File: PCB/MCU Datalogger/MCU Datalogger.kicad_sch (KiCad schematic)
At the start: 25 parts, among them U1 24LC1025, U2 24LC1025, U3 DS1337S+, U4 ATMEGA328P-AU, Y1 Crystal, Y2 Crystal

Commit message: edit component values
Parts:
- C1, C4: value C -> 0.1uF
- C2, C3: value C -> 22pF
- C5: value C_Polarized -> 100nF
- R1, R2: value R -> 330
- R3, R4, R7: value R -> 10K
- R5, R6: value R -> 4.7K
- Y1: value Crystal -> 16 MHz
- Y2: value Crystal -> 32.768 Khz
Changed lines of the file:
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@@
       (effects (font (size 1.27 1.27)) (justify left))
     )
-    (property "Value" "C" (at 163.83 81.28 0)
+    (property "Value" "22pF" (at 163.83 81.28 0)
       (effects (font (size 1.27 1.27)) (justify left))
     )
@@
       (effects (font (size 1.27 1.27)) (justify left))
     )
-    (property "Value" "R" (at 102.87 54.61 0)
+    (property "Value" "10K" (at 102.87 54.61 0)
       (effects (font (size 1.27 1.27)) (justify left))
     )
@@
       (effects (font (size 1.27 1.27)) (justify left))
     )
-    (property "Value" "R" (at 130.81 184.15 0)
+    (property "Value" "4.7K" (at 130.81 184.15 0)
       (effects (font (size 1.27 1.27)) (justify left))
     )
@@
       (effects (font (size 1.27 1.27)) (justify right))
     )
-    (property "Value" "Crystal" (at 181.61 68.58 90)
+    (property "Value" "16 MHz" (at 181.61 68.58 90)
       (effects (font (size 1.27 1.27)) (justify right))
     )
@@
       (effects (font (size 1.27 1.27)) (justify left))
     )
-    (property "Value" "R" (at 90.17 54.61 0)
+    (property "Value" "10K" (at 90.17 54.61 0)
       (effects (font (size 1.27 1.27)) (justify left))
     )
@@
       (effects (font (size 1.27 1.27)) (justify left))
     )
-    (property "Value" "C" (at 116.84 54.61 0)
+    (property "Value" "0.1uF" (at 116.84 54.61 0)
       (effects (font (size 1.27 1.27)) (justify left))
     )
@@
       (effects (font (size 1.27 1.27)) (justify left))
     )
-    (property "Value" "C_Polarized" (at 252.73 43.561 0)
+    (property "Value" "100nF" (at 252.73 43.561 0)
       (effects (font (size 1.27 1.27)) (justify left))
     )
@@
       (effects (font (size 1.27 1.27)) (justify left))
     )
-    (property "Value" "C" (at 168.91 30.48 0)
+    (property "Value" "0.1uF" (at 168.91 30.48 0)
       (effects (font (size 1.27 1.27)) (justify left))
     )
@@
       (effects (font (size 1.27 1.27)) (justify left))
     )
-    (property "Value" "R" (at 120.65 184.15 0)
+    (property "Value" "4.7K" (at 120.65 184.15 0)
       (effects (font (size 1.27 1.27)) (justify left))
     )
@@
       (effects (font (size 1.27 1.27)) (justify left))
     )
-    (property "Value" "R" (at 240.03 71.12 0)
+    (property "Value" "330" (at 240.03 71.12 0)
       (effects (font (size 1.27 1.27)) (justify left))
     )
@@
       (effects (font (size 1.27 1.27)))
     )
-    (property "Value" "R" (at 158.75 40.64 90)
+    (property "Value" "330" (at 158.75 40.64 90)
       (effects (font (size 1.27 1.27)))
     )
@@
       (effects (font (size 1.27 1.27)) (justify right))
     )
-    (property "Value" "Crystal" (at 25.4 63.5 90)
+    (property "Value" "32.768 Khz" (at 25.4 63.5 90)
       (effects (font (size 1.27 1.27)) (justify right))
     )
@@
       (effects (font (size 1.27 1.27)))
     )
-    (property "Value" "R" (at 177.8 80.01 90)
+    (property "Value" "10K" (at 177.8 80.01 90)
       (effects (font (size 1.27 1.27)))
     )
@@
       (effects (font (size 1.27 1.27)) (justify left))
     )
-    (property "Value" "C" (at 163.83 60.96 0)
-      (effects (font (size 1.27 1.27)) (justify left))
-    )
+    (property "Value" "22pF" (at 163.83 60.96 0)
+      (effects (font (size 1.27 1.27)) (justify left))
+    )

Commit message: Associate
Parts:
- BT1: footprint (none) -> Connector_PinHeader_2.54mm:PinHeader_1x02_P2.54mm_Vertical
- C1, C2, C3, C4, C5: footprint (none) -> Capacitor_SMD:C_0805_2012Metric
- D1, D2: footprint (none) -> LED_SMD:LED_0805_2012Metric
- H1, H2, H3, H4: footprint (none) -> MountingHole:MountingHole_2.1mm
- R1, R2, R3, R4, R5, R6, R7: footprint (none) -> Resistor_SMD:R_0815_2038Metric
- U1, U2: footprint (none) -> Package_SO:SOIC-8_5.23x5.23mm_P1.27mm
- U3: footprint SOIC127P600X175-8N -> DS1337S_:SOIC127P600X175-8N
- U4: footprint QFP80P900X900X120-32N -> ATMEGA328P-AU:QFP80P900X900X120-32N
- Y1, Y2: footprint (none) -> Crystal:Crystal_SMD_5032-2Pin_5.0x3.2mm_HandSoldering
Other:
- moved on the sheet: BT1, C1, C2, C3, C5, D1, D2, R1, R2, R5, R6, R7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

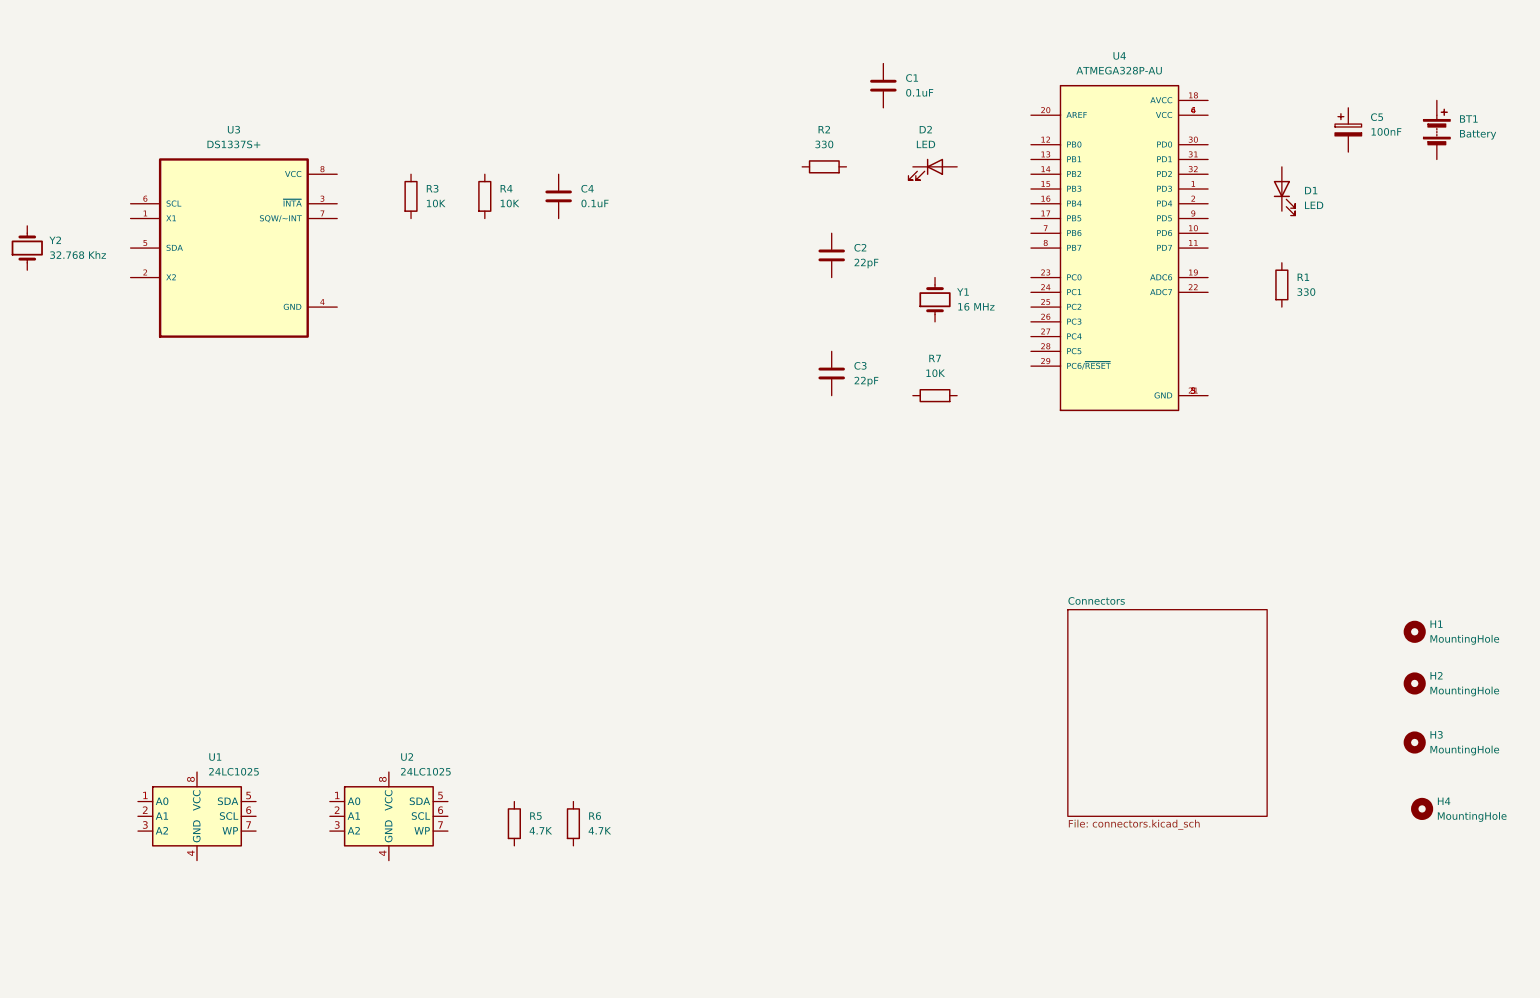
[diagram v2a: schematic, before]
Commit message: wiring of sheet 1
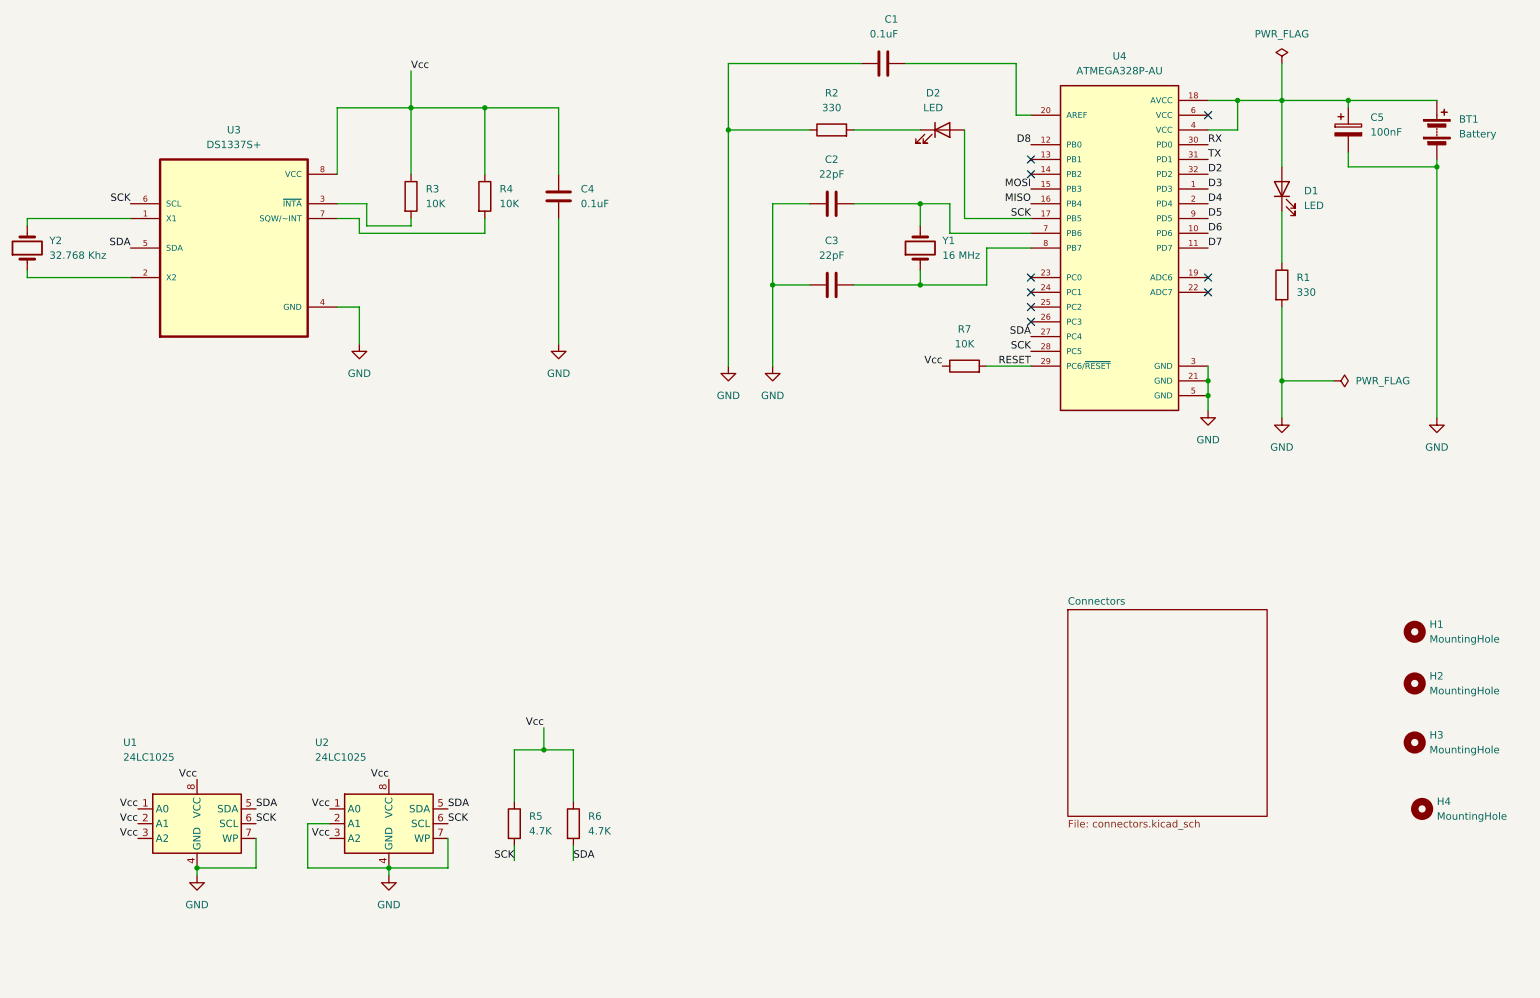
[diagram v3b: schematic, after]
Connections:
- net GND: now reaches C3.1
- net GND: now also BT1.2 (-), C1.1, C2.1, C4.2, C5.2, R1.2, R2.1, U1.4 (GND), U1.7 (WP), U2.2 (A1), U2.4 (GND), U2.7 (WP), U3.4 (GND), U4.21 (GND), U4.3 (GND), U4.5 (GND)
- net at C3.2: now also U4.8 (PB7), Y1.1
- net Vcc: now reaches R4.1
- net Vcc: now also C4.1, R3.1, R5.1, R6.1, R7.1, U1.1 (A0), U1.2 (A1), U1.3 (A2), U1.8 (VCC), U2.1 (A0), U2.3 (A2), U2.8 (VCC), U3.8 (VCC)
- net at R4.2: now also U3.7 (SQW/~INT)
- net SDA: now reaches U1.5 (SDA)
- net SDA: now also R6.2, U2.5 (SDA), U3.5 (SDA), U4.27 (PC4)
- net SCK: now reaches U1.6 (SCL)
- net SCK: now also D2.2 (A), R5.2, U2.6 (SCL), U3.6 (SCL), U4.17 (PB5), U4.28 (PC5)
- net at Y1.2: now also C2.2, U4.7 (PB6)
- net at R3.2: now also U3.3 (~{INTA})
- net at C5.1: now also BT1.1 (+), D1.2 (A), U4.18 (AVCC), U4.4 (VCC)
- net at C1.2: now also U4.20 (AREF)
- net at D2.1 (K): now also R2.2
- net at R1.1: now also D1.1 (K)
- net at Y2.1: now also U3.2 (X2)
- net at Y2.2: now also U3.1 (X1)
- net RESET: now reaches R7.2
- net RESET: now also U4.29 (PC6/~{RESET})
- net D3: now reaches U4.1 (PD3)
- net D6: now reaches U4.10 (PD6)
- net D7: now reaches U4.11 (PD7)
- net D8: now reaches U4.12 (PB0)
- net MOSI: now reaches U4.15 (PB3)
- net MISO: now reaches U4.16 (PB4)
- net D4: now reaches U4.2 (PD4)
- net RX: now reaches U4.30 (PD0)
- net TX: now reaches U4.31 (PD1)
- net D2: now reaches U4.32 (PD2)
- net at U4.6 (VCC): no longer U4.4 (VCC)
- net D5: now reaches U4.9 (PD5)
- no-connect marks 0 -> 9
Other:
- moved on the sheet: C1, C2, C3, D2, R2, R7, U1, U2, Y1

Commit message: Wiring of sheet 2
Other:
- sheet Connectors ports: added D2, D3, D4, D5, D6, D7, D8, GND, MISO, MOSI, RESET, RX, SCK, SDA, TX, Vcc; removed none
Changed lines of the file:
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@@
   (junction (at 149.86 68.58) (diameter 0) (color 0 0 0 0)
+  )
+  (junction (at 105.41 38.1) (diameter 0) (color 0 0 0 0)
   )
   (junction (at 50.8 168.91) (diameter 0) (color 0 0 0 0)
@@
     (stroke (width 0) (type default))
   )
+  (wire (pts (xy 105.41 38.1) (xy 113.03 38.1))
+    (stroke (width 0) (type default))
+  )
   (wire (pts (xy 105.41 157.48) (xy 105.41 148.59))
     (stroke (width 0) (type default))
@@
     (stroke (width 0) (type default))
   )
-  (wire (pts (xy 100.33 38.1) (xy 113.03 38.1))
+  (wire (pts (xy 100.33 38.1) (xy 105.41 38.1))
     (stroke (width 0) (type default))
   )
@@
     (stroke (width 0) (type default))
   )
+  (wire (pts (xy 105.41 33.02) (xy 105.41 38.1))
+    (stroke (width 0) (type default))
+  )
   (wire (pts (xy 156.21 54.61) (xy 149.86 54.61))
     (stroke (width 0) (type default))
@@
     (effects (font (size 1.27 1.27)) (justify left bottom))
   )
+  (label "D3" (at 213.36 124.46 0) (fields_autoplaced)
+    (effects (font (size 1.27 1.27)) (justify left bottom))
+  )
   (label "MOSI" (at 194.31 52.07 180) (fields_autoplaced)
     (effects (font (size 1.27 1.27)) (justify right bottom))
   )
+  (label "D6" (at 213.36 135.89 0) (fields_autoplaced)
+    (effects (font (size 1.27 1.27)) (justify left bottom))
+  )
   (label "Vcc" (at 179.07 82.55 180) (fields_autoplaced)
     (effects (font (size 1.27 1.27)) (justify right bottom))
@@
     (effects (font (size 1.27 1.27)) (justify right bottom))
   )
+  (label "SCK" (at 182.88 121.92 180) (fields_autoplaced)
+    (effects (font (size 1.27 1.27)) (justify right bottom))
+  )
   (label "SCK" (at 105.41 167.64 180) (fields_autoplaced)
     (effects (font (size 1.27 1.27)) (justify right bottom))
   )
+  (label "MOSI" (at 182.88 146.05 180) (fields_autoplaced)
+    (effects (font (size 1.27 1.27)) (justify right bottom))
+  )
+  (label "D2" (at 213.36 120.65 0) (fields_autoplaced)
+    (effects (font (size 1.27 1.27)) (justify left bottom))
+  )
+  (label "D8" (at 213.36 143.51 0) (fields_autoplaced)
+    (effects (font (size 1.27 1.27)) (justify left bottom))
+  )
+  (label "D7" (at 213.36 139.7 0) (fields_autoplaced)
+    (effects (font (size 1.27 1.27)) (justify left bottom))
+  )
   (label "SDA" (at 115.57 167.64 0) (fields_autoplaced)
     (effects (font (size 1.27 1.27)) (justify left bottom))
   )
+  (label "D5" (at 213.36 132.08 0) (fields_autoplaced)
+    (effects (font (size 1.27 1.27)) (justify left bottom))
+  )
   (label "SCK" (at 60.96 161.29 0) (fields_autoplaced)
     (effects (font (size 1.27 1.27)) (justify left bottom))
@@
     (effects (font (size 1.27 1.27)) (justify right bottom))
   )
+  (label "RESET" (at 182.88 153.67 180) (fields_autoplaced)
+    (effects (font (size 1.27 1.27)) (justify right bottom))
+  )
   (label "D6" (at 224.79 59.69 0) (fields_autoplaced)
     (effects (font (size 1.27 1.27)) (justify left bottom))
@@
     (effects (font (size 1.27 1.27)) (justify right bottom))
   )
+  (label "Vcc" (at 182.88 111.76 180) (fields_autoplaced)
+    (effects (font (size 1.27 1.27)) (justify right bottom))
+  )
   (label "Vcc" (at 73.66 158.75 180) (fields_autoplaced)
     (effects (font (size 1.27 1.27)) (justify right bottom))
@@
     (effects (font (size 1.27 1.27)) (justify right bottom))
   )
+  (label "D4" (at 213.36 128.27 0) (fields_autoplaced)
+    (effects (font (size 1.27 1.27)) (justify left bottom))
+  )
   (label "SDA" (at 93.98 158.75 0) (fields_autoplaced)
     (effects (font (size 1.27 1.27)) (justify left bottom))
@@
     (effects (font (size 1.27 1.27)) (justify right bottom))
   )
+  (label "SDA" (at 182.88 125.73 180) (fields_autoplaced)
+    (effects (font (size 1.27 1.27)) (justify right bottom))
+  )
+  (label "RX" (at 182.88 134.62 180) (fields_autoplaced)
+    (effects (font (size 1.27 1.27)) (justify right bottom))
+  )
+  (label "MISO" (at 182.88 149.86 180) (fields_autoplaced)
+    (effects (font (size 1.27 1.27)) (justify right bottom))
+  )
   (label "D4" (at 224.79 54.61 0) (fields_autoplaced)
     (effects (font (size 1.27 1.27)) (justify left bottom))
@@
     (effects (font (size 1.27 1.27)) (justify left bottom))
   )
+  (label "TX" (at 182.88 138.43 180) (fields_autoplaced)
+    (effects (font (size 1.27 1.27)) (justify right bottom))
+  )
   (label "MISO" (at 194.31 54.61 180) (fields_autoplaced)
     (effects (font (size 1.27 1.27)) (justify right bottom))
@@
         (path "/551e4e84-b335-467b-846f-a0d4917bd2bc"
           (reference "#PWR09") (unit 1)
+        )
+      )
+    )
+  )
+  (symbol (lib_id "power:PWR_FLAG") (at 105.41 33.02 0) (unit 1)
+    (in_bom yes) (on_board yes) (dnp no) (fields_autoplaced)
+    (property "Reference" "#FLG03" (at 105.41 31.115 0)
+      (effects (font (size 1.27 1.27)) hide)
+    )
+    (property "Value" "PWR_FLAG" (at 105.41 27.94 0)
+      (effects (font (size 1.27 1.27)))
+    )
+    (property "Footprint" "" (at 105.41 33.02 0)
+      (effects (font (size 1.27 1.27)) hide)
+    )
+    (property "Datasheet" "~" (at 105.41 33.02 0)
+      (effects (font (size 1.27 1.27)) hide)
+    )
+    (pin "1")
+    (instances
+      (project "MCU Datalogger"
+        (path "/551e4e84-b335-467b-846f-a0d4917bd2bc"
+          (reference "#FLG03") (unit 1)
         )
       )
@@
         (path "/551e4e84-b335-467b-846f-a0d4917bd2bc"
           (reference "R2") (unit 1)
+        )
+      )
+    )
+  )
+  (symbol (lib_id "power:GND") (at 182.88 114.3 270) (unit 1)
+    (in_bom yes) (on_board yes) (dnp no) (fields_autoplaced)
+    (property "Reference" "#PWR010" (at 176.53 114.3 0)
+      (effects (font (size 1.27 1.27)) hide)
+    )
+    (property "Value" "GND" (at 179.07 114.3 90)
+      (effects (font (size 1.27 1.27)) (justify right))
+    )
+    (property "Footprint" "" (at 182.88 114.3 0)
+      (effects (font (size 1.27 1.27)) hide)
+    )
+    (property "Datasheet" "" (at 182.88 114.3 0)
+      (effects (font (size 1.27 1.27)) hide)
+    )
+    (pin "1")
+    (instances
+      (project "MCU Datalogger"
+        (path "/551e4e84-b335-467b-846f-a0d4917bd2bc"
+          (reference "#PWR010") (unit 1)
         )
       )
@@
     )
   )
-  (sheet (at 200.66 124.46) (size 34.29 35.56) (fields_autoplaced)
+  (sheet (at 182.88 107.95) (size 30.48 49.53) (fields_autoplaced)
     (stroke (width 0.1524) (type solid))
     (fill (color 0 0 0 0.0000))
-    (property "Sheetname" "Connectors" (at 200.66 123.7484 0)
+    (property "Sheetname" "Connectors" (at 182.88 107.2384 0)
       (effects (font (size 1.27 1.27)) (justify left bottom))
     )
-    (property "Sheetfile" "connectors.kicad_sch" (at 200.66 160.6046 0)
+    (property "Sheetfile" "connectors.kicad_sch" (at 182.88 158.0646 0)
       (effects (font (size 1.27 1.27)) (justify left top))
     )
-    (instances
+    (pin "RX" input (at 182.88 134.62 180)
+      (effects (font (size 1.27 1.27)) (justify left))
+    )
+    (pin "Vcc" passive (at 182.88 111.76 180)
+      (effects (font (size 1.27 1.27)) (justify left))
+    )
+    (pin "TX" output (at 182.88 138.43 180)
+      (effects (font (size 1.27 1.27)) (justify left))
+    )
+    (pin "GND" passive (at 182.88 114.3 180)
+      (effects (font (size 1.27 1.27)) (justify left))
+    )
+    (pin "D4" bidirectional (at 213.36 128.27 0)
+      (effects (font (size 1.27 1.27)) (justify right))
+    )
+    (pin "D2" bidirectional (at 213.36 120.65 0)
+      (effects (font (size 1.27 1.27)) (justify right))
+    )
+    (pin "D8" bidirectional (at 213.36 143.51 0)
+      (effects (font (size 1.27 1.27)) (justify right))
+    )
+    (pin "SCK" passive (at 182.88 121.92 180)
+      (effects (font (size 1.27 1.27)) (justify left))
+    )
+    (pin "SDA" bidirectional (at 182.88 125.73 180)
+      (effects (font (size 1.27 1.27)) (justify left))
+    )
+    (pin "D3" bidirectional (at 213.36 124.46 0)
+      (effects (font (size 1.27 1.27)) (justify right))
+    )
+    (pin "D5" bidirectional (at 213.36 132.08 0)
+      (effects (font (size 1.27 1.27)) (justify right))
+    )
+    (pin "D6" bidirectional (at 213.36 135.89 0)
+      (effects (font (size 1.27 1.27)) (justify right))
+    )
+    (pin "D7" bidirectional (at 213.36 139.7 0)
+      (effects (font (size 1.27 1.27)) (justify right))
+    )
+    (pin "MOSI" input (at 182.88 146.05 180)
+      (effects (font (size 1.27 1.27)) (justify left))
+    )
+    (pin "MISO" output (at 182.88 149.86 180)
+      (effects (font (size 1.27 1.27)) (justify left))
+    )
+    (pin "RESET" passive (at 182.88 153.67 180)
+      (effects (font (size 1.27 1.27)) (justify left))
+    )
+    (instances
